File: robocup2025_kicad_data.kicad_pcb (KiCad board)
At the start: 4 copper layers, 15 parts, among them M7 Motor_Servo, U2 ESP32-DEVKITC-32E

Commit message: changed place
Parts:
- moved F1 48.8 mm to (142.0, 117.6)
- moved U6 0.58 mm to (140.5, 113.4)
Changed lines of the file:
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@@
 	(footprint "robo:voltmeter"
 		(layer "F.Cu")
-		(at 139.958 113.7)
+		(at 140.462 113.411)
 		(property "Reference" "U6"
 			(at 0 -0.5 0)
@@
 	(footprint "robo:fuse_holder"
 		(layer "F.Cu")
-		(at 190.754 116.87)
+		(at 141.986 117.602)
 		(property "Reference" "F1"
 			(at 0 -0.5 0)

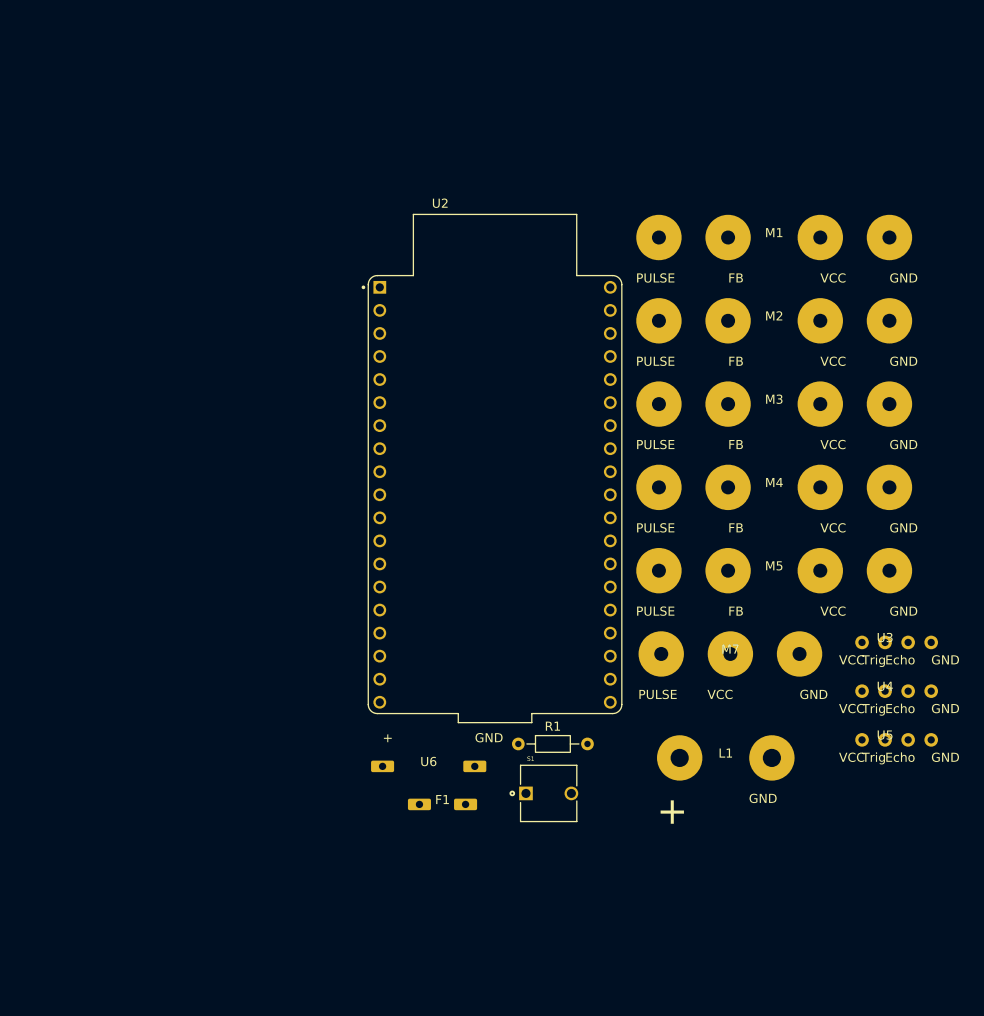
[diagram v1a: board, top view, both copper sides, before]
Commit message: new edge on pcb
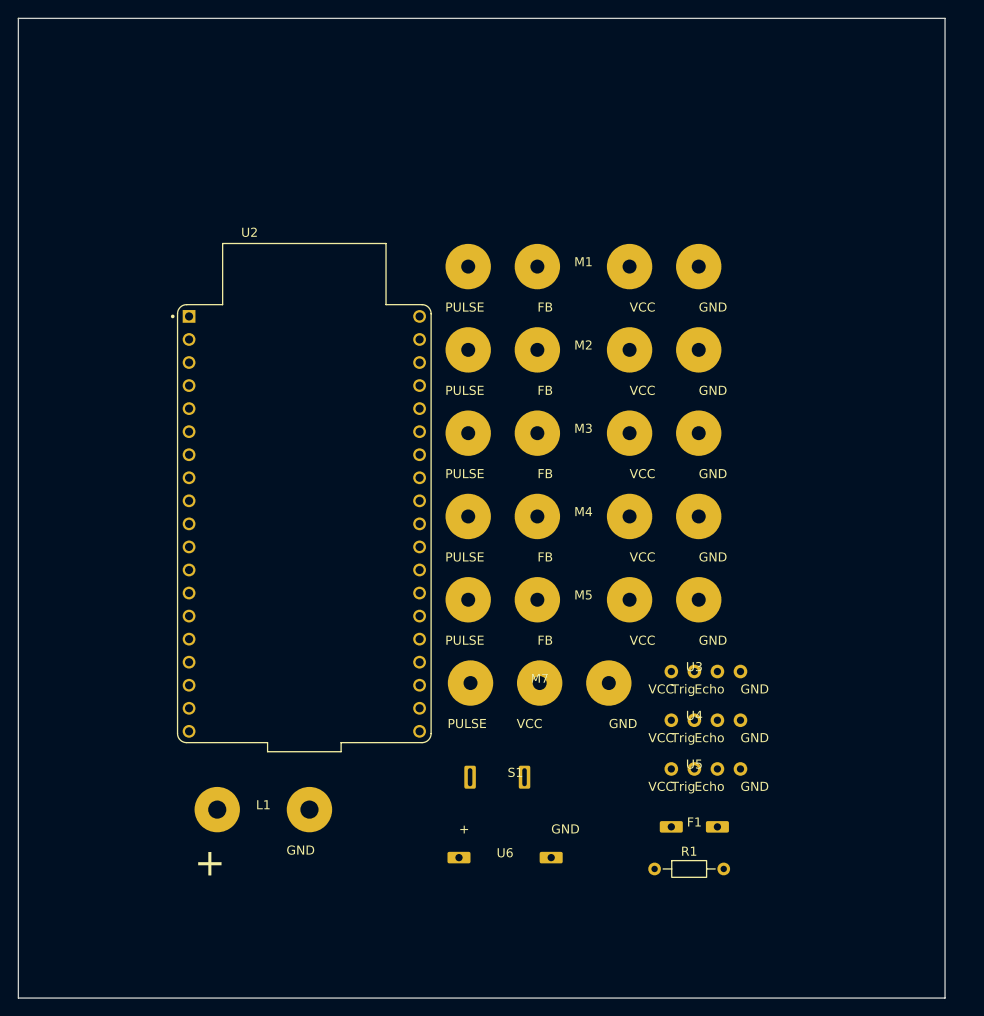
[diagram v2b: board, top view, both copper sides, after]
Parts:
- S1: footprint robo:tactile switch -> robo:DS-850K-S-ON
- moved L1 51.3 mm to (122.2, 118.2)
- moved F1 27.9 mm to (169.7, 120.1)
- moved U2 21.3 mm to (126.8, 86.7)
- moved M1 21.3 mm to (157.5, 58.3)
- moved M2 21.3 mm to (157.5, 67.5)
- moved M3 21.3 mm to (157.5, 76.7)
- moved M4 21.3 mm to (157.5, 85.9)
- moved M5 21.3 mm to (157.5, 95.0)
- moved M7 21.3 mm to (152.7, 104.2)
- moved U3 21.3 mm to (169.7, 103.0)
- moved U4 21.3 mm to (169.7, 108.3)
- moved U5 21.3 mm to (169.7, 113.7)
- moved R1 20.4 mm to (165.4, 124.7)
- moved U6 13.1 mm to (148.9, 123.5)
- moved S1 4.07 mm to (150.0, 114.6)
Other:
- board outline added: 102.1 x 107.9 mm

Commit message: created through hole
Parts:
- added REF**: 2mm diameter through hole, robo:2mm diameter through hole, F.Cu at (109.0, 130.0)
- added REF**: 2mm diameter through hole, robo:2mm diameter through hole, F.Cu at (109.0, 40.0)
- added REF**: 2mm diameter through hole, robo:2mm diameter through hole, F.Cu at (189.0, 40.0)
- added REF**: 2mm diameter through hole, robo:2mm diameter through hole, F.Cu at (189.0, 130.0)

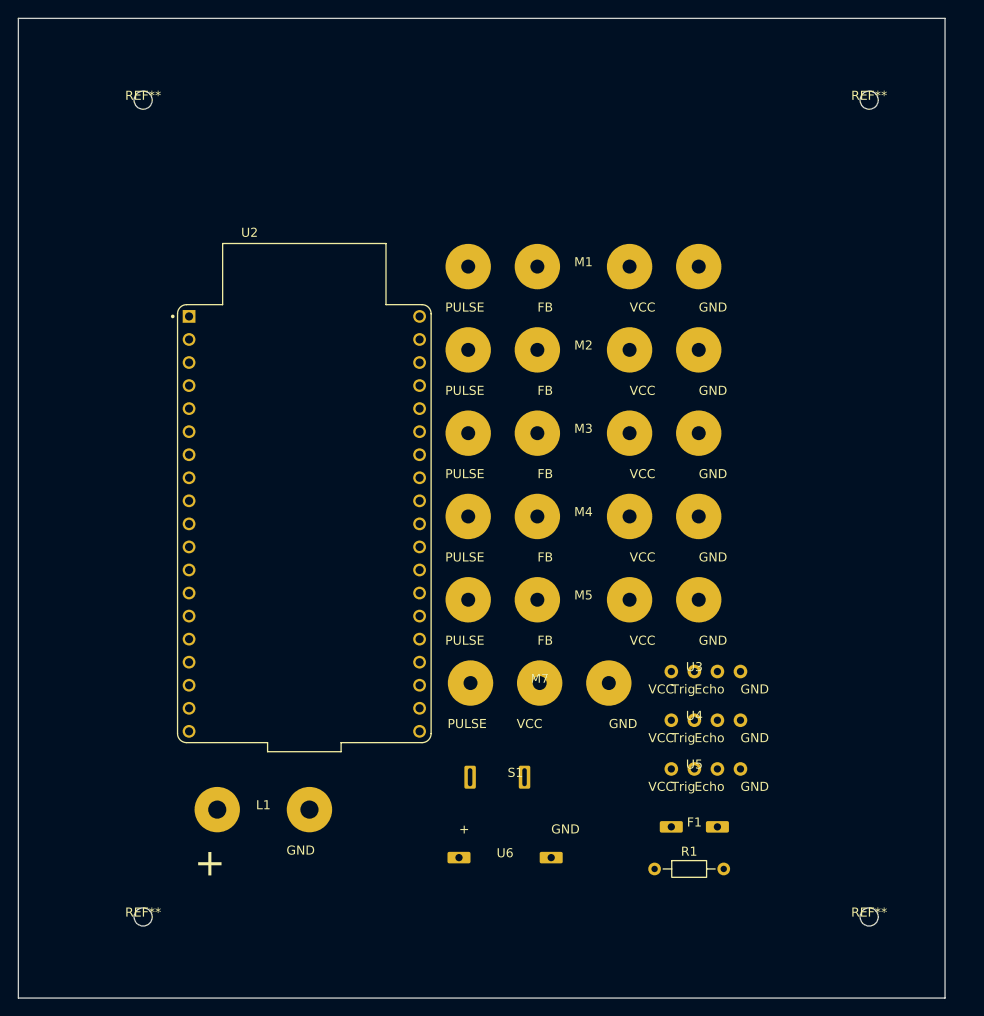
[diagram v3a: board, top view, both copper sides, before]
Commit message: removed 2mm throughhole
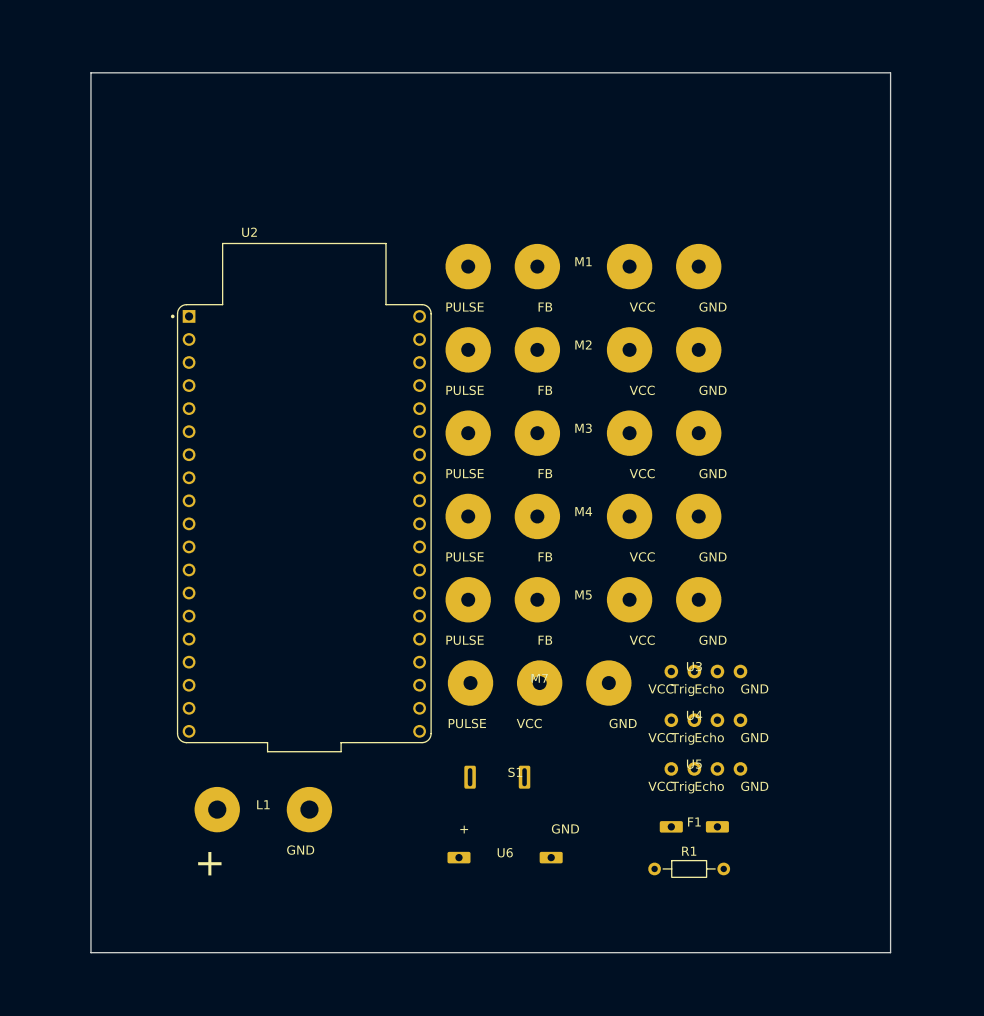
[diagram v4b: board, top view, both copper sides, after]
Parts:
- removed REF** (x4): 2mm diameter through hole, robo:2mm diameter through hole
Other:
- board size 102.1 x 107.9 mm -> 88.1 x 96.9 mm

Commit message: placed 4mm through hole
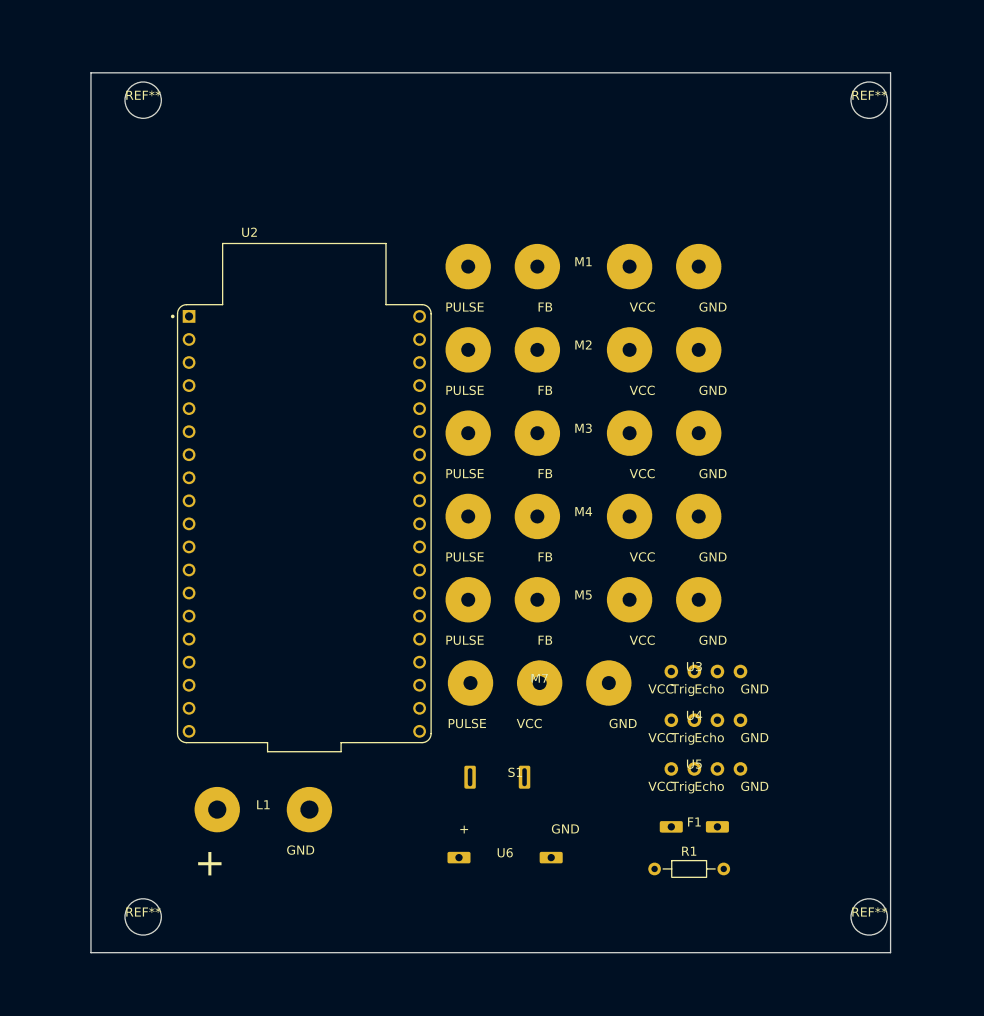
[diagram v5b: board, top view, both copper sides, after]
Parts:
- added REF**: 4mm diameter through hole, robo:4mm diameter through hole, F.Cu at (189.0, 130.0)
- added REF**: 4mm diameter through hole, robo:4mm diameter through hole, F.Cu at (189.0, 40.0)
- added REF**: 4mm diameter through hole, robo:4mm diameter through hole, F.Cu at (109.0, 130.0)
- added REF**: 4mm diameter through hole, robo:4mm diameter through hole, F.Cu at (109.0, 40.0)

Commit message: filled gnd and lipo
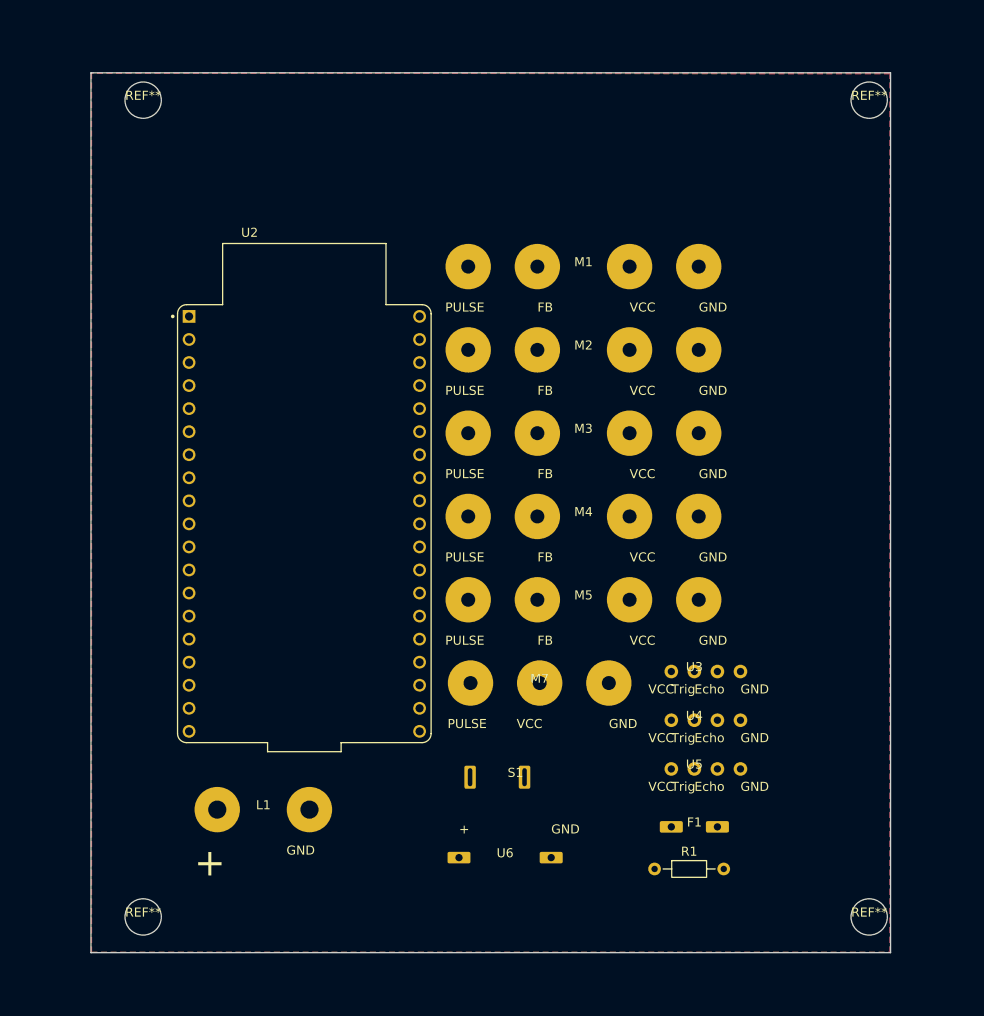
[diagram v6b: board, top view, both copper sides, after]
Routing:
- added copper zone on F.Cu, net GND
- added copper zone on B.Cu, net LiPo+
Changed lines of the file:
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@@
+		)
+	)
+	(zone
+		(net 2)
+		(net_name "GND")
+		(layer "F.Cu")
+		(hatch edge 0.5)
+		(connect_pads
+			(clearance 0.5)
+		)
+		(min_thickness 0.25)
+		(filled_areas_thickness no)
+		(fill yes
+			(thermal_gap 0.5)
+			(thermal_bridge_width 0.5)
+		)
+		(polygon
+			(pts
+				(xy 103.3 37) (xy 103.3 133.9) (xy 191.3 133.9) (xy 191.3 37) (xy 191.3 37.1)
+			)
+		)
+	)
+	(zone
+		(net 1)
+		(net_name "LiPo+")
+		(layer "B.Cu")
+		(hatch edge 0.5)
+		(priority 1)
+		(connect_pads
+			(clearance 0.5)
+		)
+		(min_thickness 0.25)
+		(filled_areas_thickness no)
+		(fill yes
+			(thermal_gap 0.5)
+			(thermal_bridge_width 0.5)
+		)
+		(polygon
+			(pts
+				(xy 103.3 133.9) (xy 191.3 133.9) (xy 191.3 37) (xy 103.3 37)
+			)
 		)
 	)

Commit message: changed reference
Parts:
- renumbered REF** to H1, REF** to H2, REF** to H3, REF** to H4
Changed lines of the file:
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@@
 		(layer "F.Cu")
 		(at 189 130)
-		(property "Reference" "REF**"
+		(property "Reference" "H3"
 			(at 0 -0.5 0)
 			(unlocked yes)
@@
 		(layer "F.Cu")
 		(at 189 40)
-		(property "Reference" "REF**"
+		(property "Reference" "H4"
 			(at 0 -0.5 0)
 			(unlocked yes)
@@
 		(layer "F.Cu")
 		(at 109 130)
-		(property "Reference" "REF**"
+		(property "Reference" "H2"
 			(at 0 -0.5 0)
 			(unlocked yes)
@@
 		(layer "F.Cu")
 		(at 109 40)
-		(property "Reference" "REF**"
+		(property "Reference" "H1"
 			(at 0 -0.5 0)
 			(unlocked yes)

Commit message: pcb done!
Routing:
- net ESP32_3.3: track 0.00 -> 121.8 mm, vias 0 -> 2
- net ultrasonic_echo2: track 0.00 -> 75.8 mm, vias 0 -> 1
- net ESP32_21: track 0.00 -> 72.9 mm
- net arm_feedback: track 0.00 -> 72.3 mm, vias 0 -> 1
- net ultrasonic_echo3: track 0.00 -> 70.2 mm
- net ultrasonic_trig3: track 0.00 -> 68.3 mm
- net tyre_pulse_1: track 0.00 -> 63.4 mm, vias 0 -> 1
- net Net-(L1-+): track 0.00 -> 60.9 mm
- net ultrasonic_trig2: track 0.00 -> 60.4 mm, vias 0 -> 1
- net arm_wire_SIG: track 0.00 -> 58.5 mm, vias 0 -> 1
- net tyre_pulse_2: track 0.00 -> 55.5 mm, vias 0 -> 1
- net ultrasonic_echo1: track 0.00 -> 44.4 mm
- net ultrasonic_trig1: track 0.00 -> 40.2 mm
- net tyre_pulse_3: track 0.00 -> 31.9 mm
- net tyre_pulse_4: track 0.00 -> 8.12 mm
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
